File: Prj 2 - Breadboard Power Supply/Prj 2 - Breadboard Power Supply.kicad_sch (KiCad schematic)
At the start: 16 parts, among them J1 Conn_01x02_Pin, J2 Conn_01x03_Pin, J3 Conn_01x02_Pin, J4 Conn_01x03_Pin, J5 Screw_Terminal_01x02, J6 Barrel_Jack_Switch, U1 LM7805_TO220, U2 LM317_TO-220

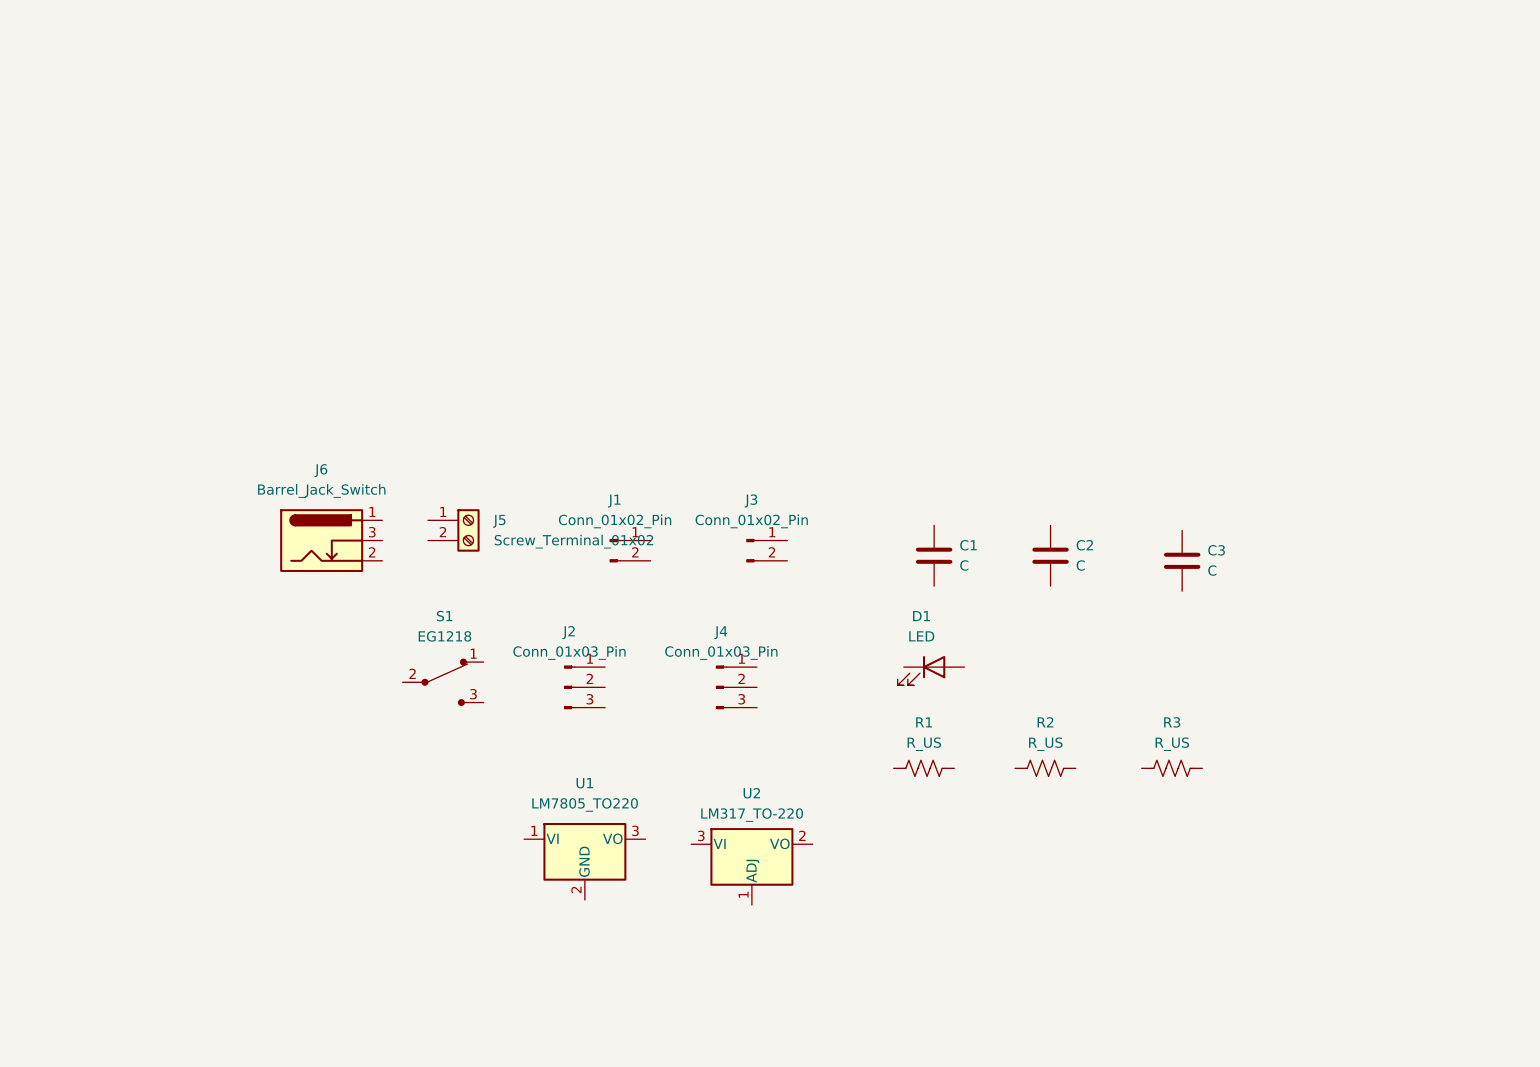
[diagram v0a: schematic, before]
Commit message: add the components and move them into the areas where they will fit together
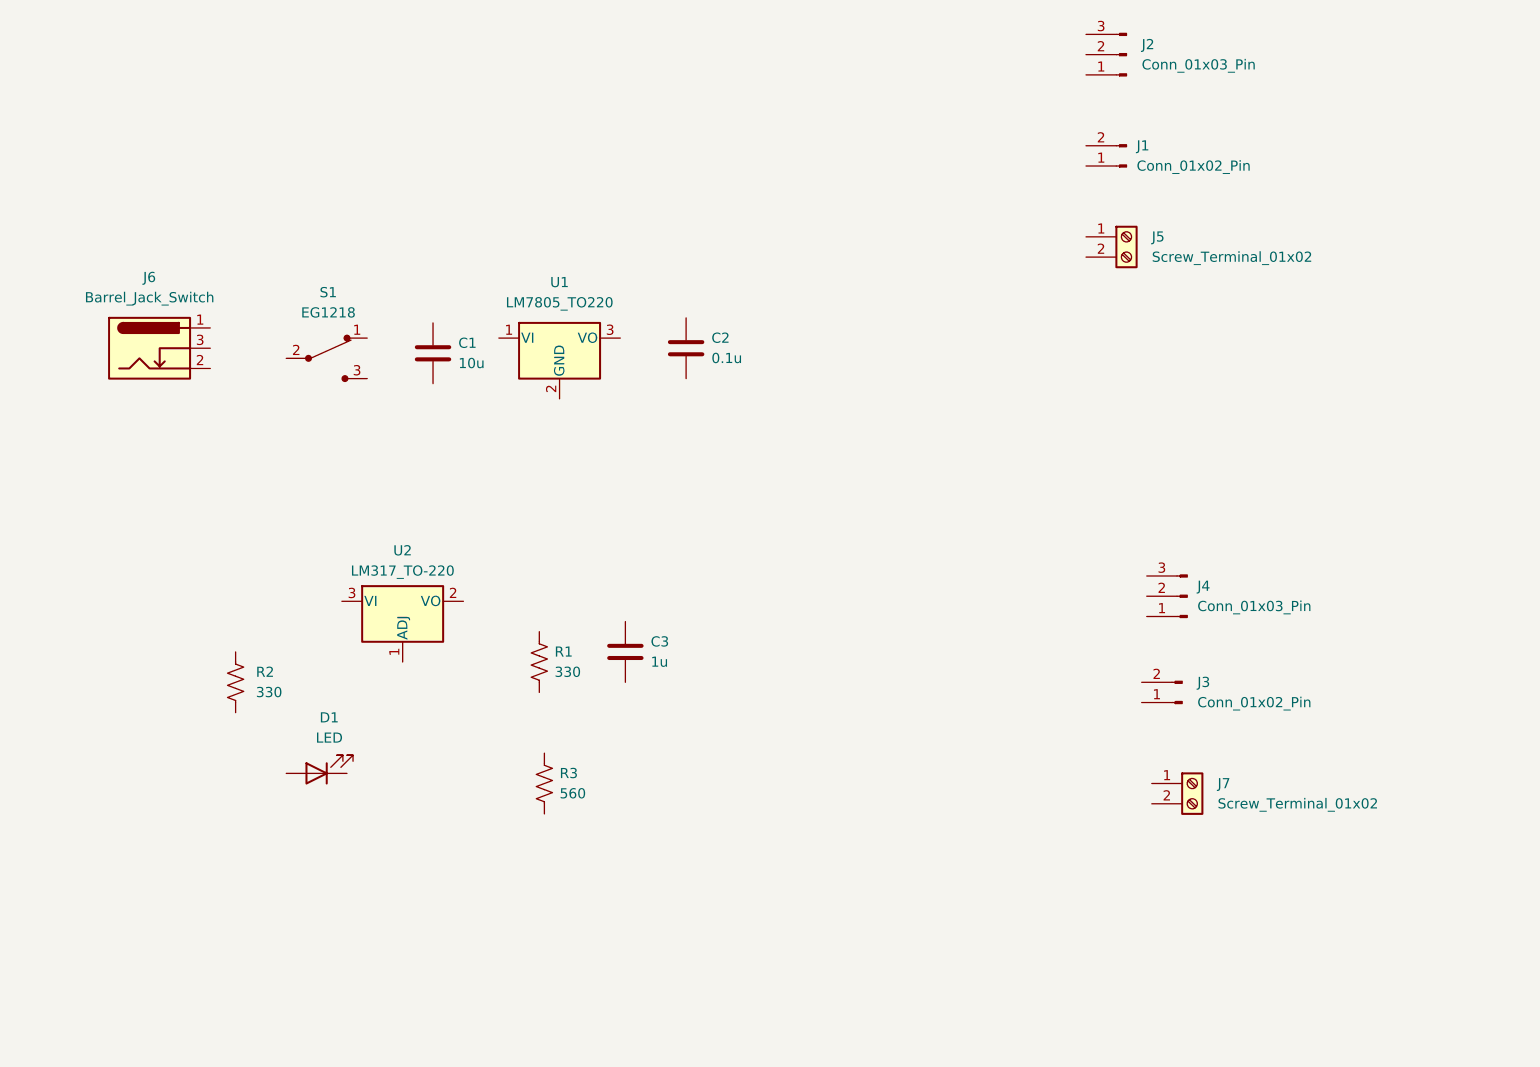
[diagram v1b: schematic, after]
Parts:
- added J7: Screw_Terminal_01x02, symbol Connector:Screw_Terminal_01x02
- C1: value C -> 10u
- C2: value C -> 0.1u
- C3: value C -> 1u
- R1, R2: value R_US -> 330
- R3: value R_US -> 560
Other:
- moved on the sheet: C1, C2, C3, D1, J1, J2, J3, J4, J5, J6, R1, R2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

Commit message: associate all the components with pads
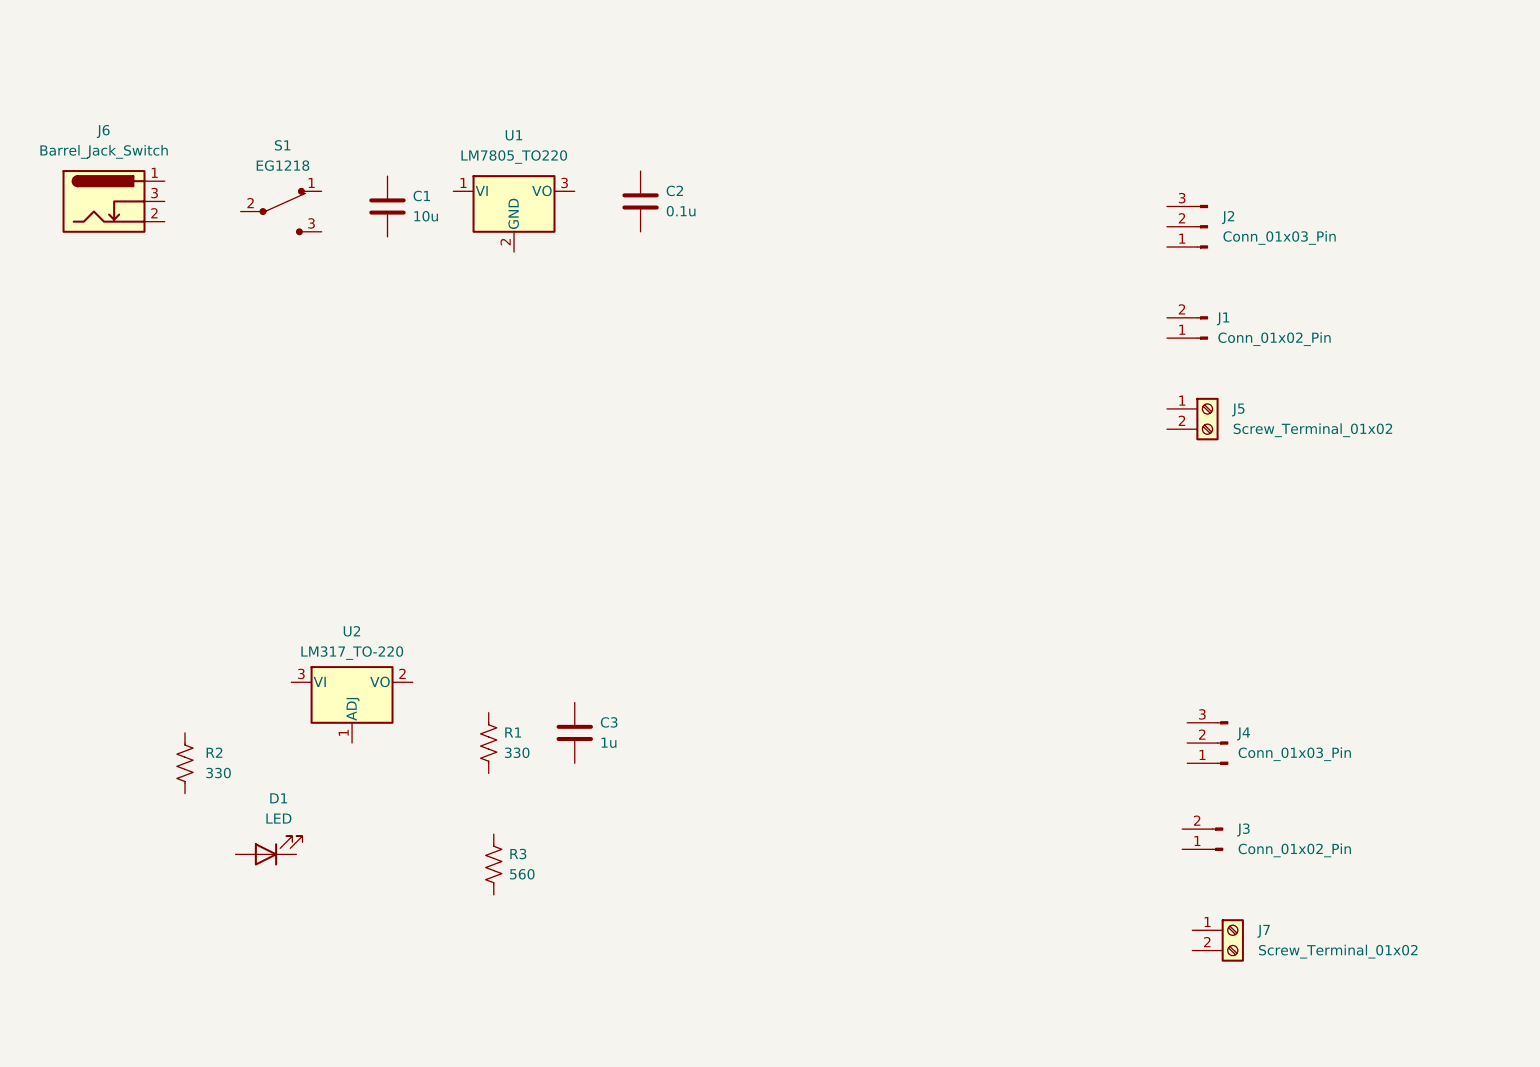
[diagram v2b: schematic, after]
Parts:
- C1, C2, C3: footprint (none) -> Capacitor_THT:C_Disc_D5.0mm_W2.5mm_P2.50mm
- D1: footprint (none) -> LED_THT:LED_D5.0mm
- J1, J3: footprint (none) -> Connector_PinHeader_2.54mm:PinHeader_1x02_P2.54mm_Vertical
- J2, J4: footprint (none) -> Connector_PinHeader_2.54mm:PinHeader_1x03_P2.54mm_Vertical
- J5, J7: footprint (none) -> TerminalBlock:TerminalBlock_bornier-2_P5.08mm
- J6: footprint (none) -> Connector_BarrelJack:BarrelJack_Horizontal
- R1, R2, R3: footprint (none) -> Resistor_THT:R_Axial_DIN0204_L3.6mm_D1.6mm_P7.62mm_Horizontal
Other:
- moved on the sheet: C1, C2, C3, D1, J1, J2, J3, J4, J5, J6, J7, R1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

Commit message: final schematic for v1 of the power supply
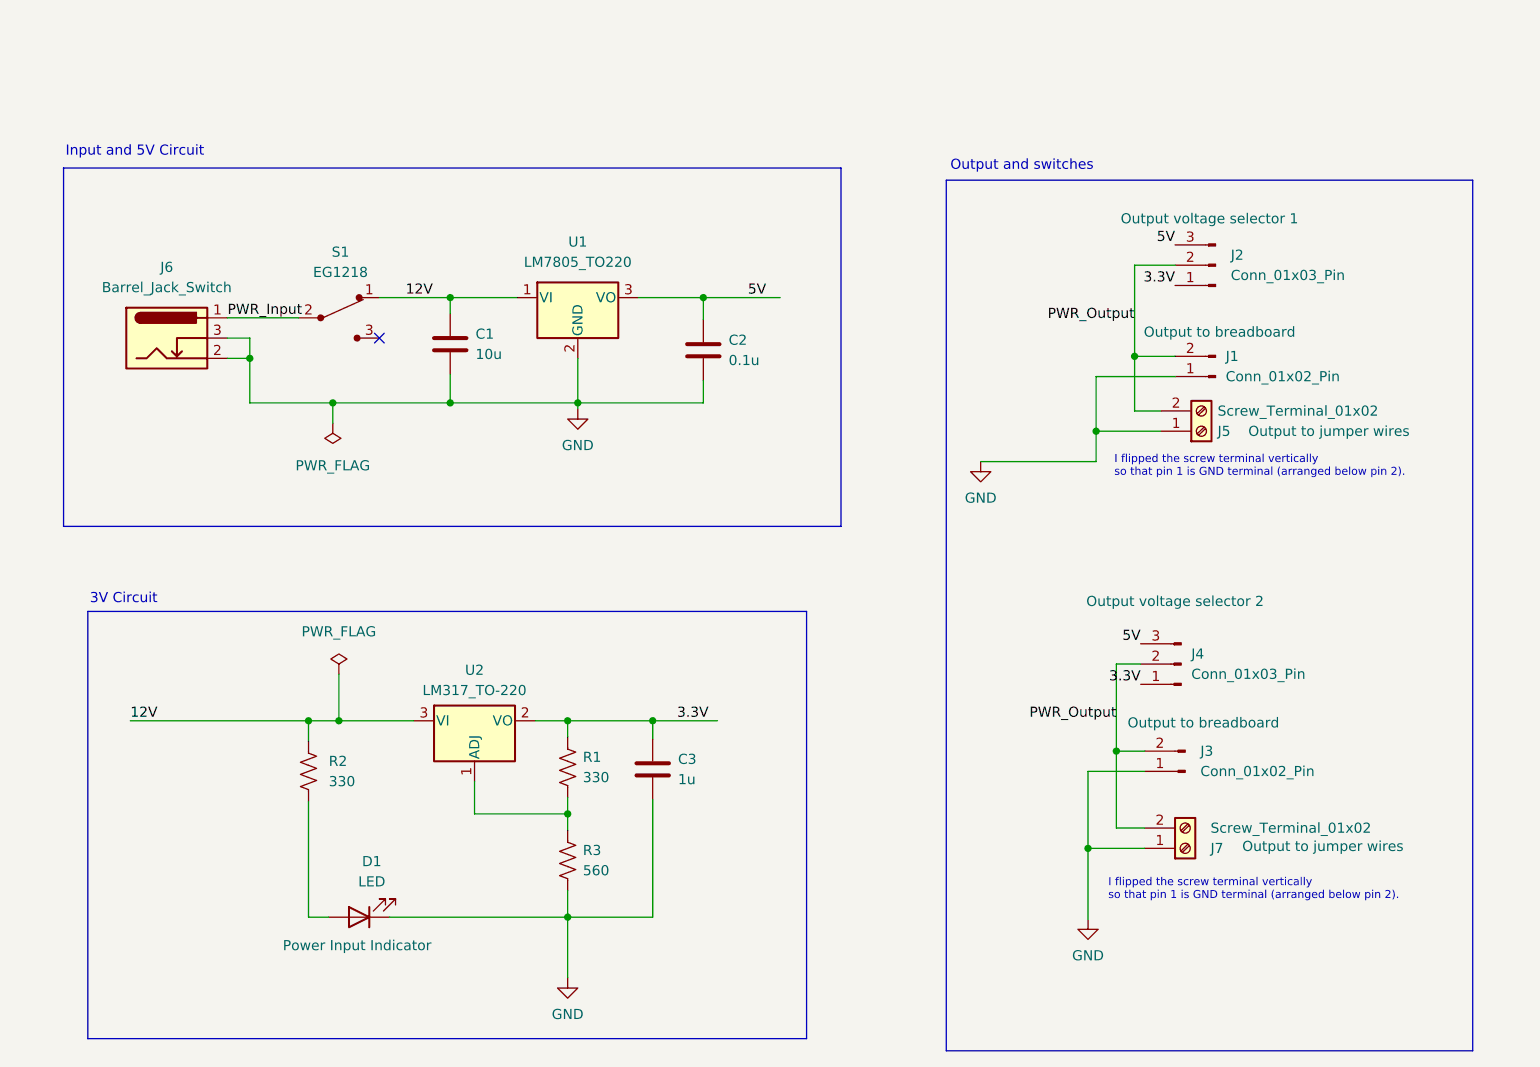
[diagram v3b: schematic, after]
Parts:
- D1: Purpose (none) -> Power Input Indicator
- J1, J3: Purpose (none) -> Output to breadboard
- J2: Purpose (none) -> Output voltage selector 1
- J4: Purpose (none) -> Output voltage selector 2
- J5, J7: Purpose (none) -> Output to jumper wires
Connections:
- net at R2.1: now also D1.2 (A)
- net 12V: now reaches R2.2
- net 12V: now also C1.1, S1.1, U1.1 (VI), U2.3 (VI)
- net 3.3V: now reaches C3.1
- net 3.3V: now also J2.1 (Pin_1), J4.1 (Pin_1), R1.2, U2.2 (VO)
- net GND: now reaches C3.2
- net GND: now also C1.2, C2.2, D1.1 (K), J1.1 (Pin_1), J3.1 (Pin_1), J5.1 (Pin_1), J6.2, J6.3, J7.1 (Pin_1), R3.1, U1.2 (GND)
- net at U2.1 (ADJ): now also R1.1, R3.2
- net PWR_Output: now reaches J2.2 (Pin_2)
- net PWR_Output: now also J1.2 (Pin_2), J3.2 (Pin_2), J4.2 (Pin_2), J5.2 (Pin_2), J7.2 (Pin_2)
- net 5V: now reaches J2.3 (Pin_3)
- net 5V: now also C2.1, J4.3 (Pin_3), U1.3 (VO)
- net PWR_Input: now reaches S1.2
- net PWR_Input: now also J6.1
- no-connect marks 0 -> 1
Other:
- note added: "3V Circuit"
- note added: "I flipped the screw terminal vertically so that pin 1 is GND terminal (arranged below pin 2)."
- note added: "Input and 5V Circuit"
- note added: "Output and switches"
- moved on the sheet: C1, C2, C3, D1, J1, J2, J3, J4, J5, J6, J7, R1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
